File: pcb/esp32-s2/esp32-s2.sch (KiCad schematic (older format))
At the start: 31 parts, among them J1 BATT, J2 HALL-CONN, Q1 BC817, Q2 BC807, SW1 WIFI-Config, SW2 RST, U1 XC6220, U2 ESP32-S2-WROOM

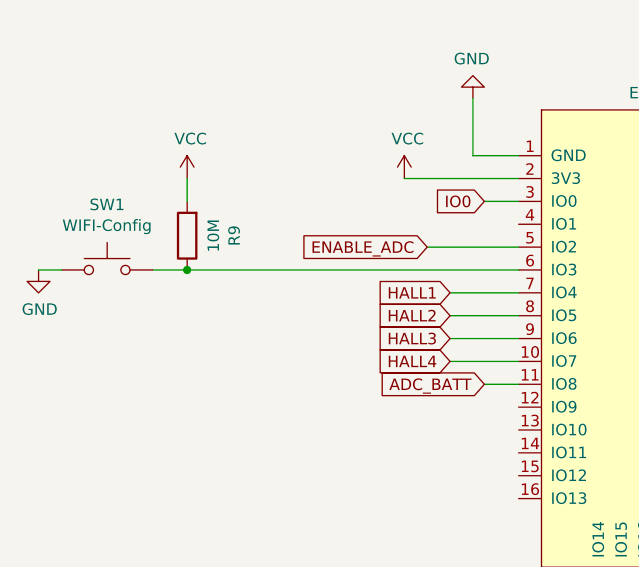
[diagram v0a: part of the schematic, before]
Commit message: update pcb for esp32s2
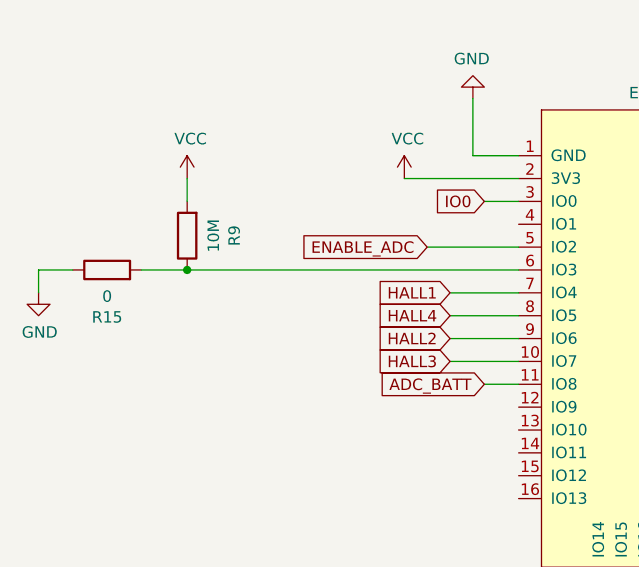
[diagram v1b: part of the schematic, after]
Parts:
- removed SW1: WIFI-Config, SMDButton:SMD_Button, symbol Switch:SW_Push
- added R15: 0, Resistor_SMD:R_0805_2012Metric, symbol Device:R
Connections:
- net GND: now also R15.1
- net HALL2: now also U2.9 (IO6); no longer U2.8 (IO5)
- net HALL3: now also U2.10 (IO7); no longer U2.9 (IO6)
- net HALL4: now also U2.8 (IO5); no longer U2.10 (IO7)
- net at R9.1, U2.6 (IO3): now also R15.2
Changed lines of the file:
@@
 HALL1
 Text GLabel 2400 3250 0    50   Input ~ 0
+HALL4
+Text GLabel 2400 3350 0    50   Input ~ 0
 HALL2
-Text GLabel 2400 3350 0    50   Input ~ 0
+Text GLabel 2400 3450 0    50   Input ~ 0
 HALL3
-Text GLabel 2400 3450 0    50   Input ~ 0
-HALL4
 Wire Wire Line
 	2700 3150 2400 3150
@@
 	9450 1000 9350 1000
 $Comp
-L Switch:SW_Push SW1
-U 1 1 5FF79AF1
-P 900 3050
-F 0 "SW1" H 900 3335 50  0000 C CNN
-F 1 "WIFI-Config" H 900 3244 50  0000 C CNN
-F 2 "SMDButton:SMD_Button" H 900 3250 50  0001 C CNN
-F 3 "~" H 900 3250 50  0001 C CNN
-	1    900  3050
-	1    0    0    -1
-$EndComp
-$Comp
-L power:GND #PWR01
-U 1 1 5FF7AC8D
-P 600 3050
-F 0 "#PWR01" H 600 2800 50  0001 C CNN
-F 1 "GND" H 605 2877 50  0000 C CNN
-F 2 "" H 600 3050 50  0001 C CNN
-F 3 "" H 600 3050 50  0001 C CNN
-	1    600  3050
-	1    0    0    -1
-$EndComp
-$Comp
 L Device:R R9
 U 1 1 5FF7B7F9
@@
 Wire Wire Line
 	2700 3050 1250 3050
-Wire Wire Line
-	1250 3050 1100 3050
-Connection ~ 1250 3050
-Wire Wire Line
-	700  3050 600  3050
 Wire Wire Line
 	1250 2750 1250 2650
@@
 Text Label 4850 4050 0    50   ~ 0
 Blue
+$Comp
+L power:GND #PWR01
+U 1 1 5FFB254B
+P 600 3150
+F 0 "#PWR01" H 600 2900 50  0001 C CNN
+F 1 "GND" H 605 2977 50  0000 C CNN
+F 2 "" H 600 3150 50  0001 C CNN
+F 3 "" H 600 3150 50  0001 C CNN
+	1    600  3150
+	1    0    0    -1
+$EndComp
+$Comp
+L Device:R R15
+U 1 1 5FFC2892
+P 900 3050
+F 0 "R15" V 693 3050 50  0000 C CNN
+F 1 "0" V 784 3050 50  0000 C CNN
+F 2 "Resistor_SMD:R_0805_2012Metric" V 830 3050 50  0001 C CNN
+F 3 "~" H 900 3050 50  0001 C CNN
+	1    900  3050
+	0    -1   -1   0
+$EndComp
+Wire Wire Line
+	1250 3050 1050 3050
+Connection ~ 1250 3050
+Wire Wire Line
+	750  3050 600  3050
+Wire Wire Line
+	600  3050 600  3150
 $EndSCHEMATC

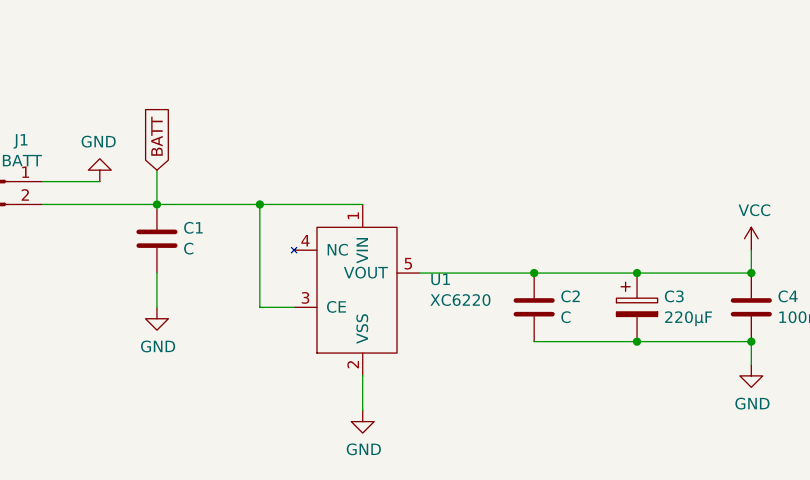
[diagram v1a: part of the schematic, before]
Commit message: update pcb: add cap values
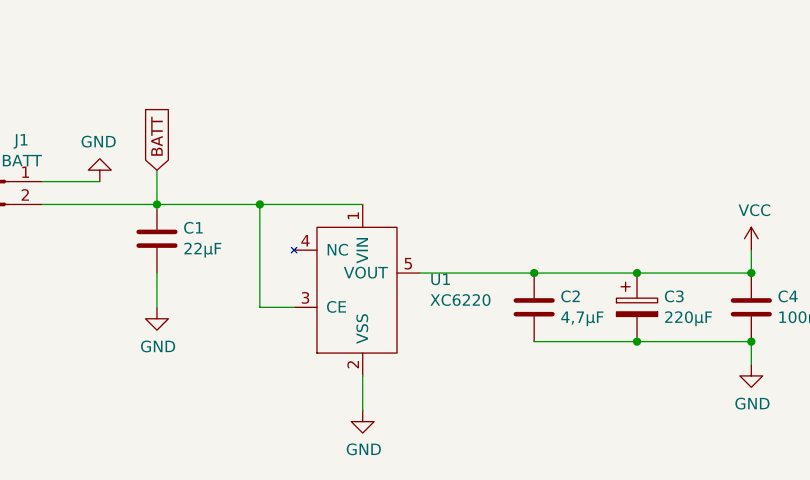
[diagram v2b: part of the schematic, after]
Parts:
- C1: value C -> 22µF
- C2: value C -> 4,7µF
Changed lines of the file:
@@
 P 1250 6100
 F 0 "C1" H 1365 6146 50  0000 L CNN
-F 1 "C" H 1365 6055 50  0000 L CNN
+F 1 "22µF" H 1365 6055 50  0000 L CNN
 F 2 "Capacitor_SMD:C_0805_2012Metric" H 1288 5950 50  0001 C CNN
 F 3 "~" H 1250 6100 50  0001 C CNN
@@
 P 2900 6400
 F 0 "C2" H 3015 6446 50  0000 L CNN
-F 1 "C" H 3015 6355 50  0000 L CNN
+F 1 "4,7µF" H 3015 6355 50  0000 L CNN
 F 2 "Capacitor_SMD:C_0805_2012Metric" H 2938 6250 50  0001 C CNN
 F 3 "~" H 2900 6400 50  0001 C CNN

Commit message: add todo
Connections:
- net IO18: now reaches R1.2, U2.21 (IO18)
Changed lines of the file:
@@
 Wire Wire Line
 	600  3050 600  3150
+Text Label 3650 4700 0    50   ~ 0
+IO18
 $EndSCHEMATC
